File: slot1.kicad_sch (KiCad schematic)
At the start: 1 part

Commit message: board layout
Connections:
- net AD1: now also PL1.a3 (Pin_a3); no longer PL1.b3 (Pin_b3)
- net Chroma: now also PL1.a2 (Pin_a2); no longer PL1.b2 (Pin_b2)
- net GND: now also PL1.b3 (Pin_b3); no longer PL1.a3 (Pin_a3)
- net Luma: now also PL1.b2 (Pin_b2); no longer PL1.a2 (Pin_a2)
- net VCLK: now reaches PL1.a38 (Pin_a38)
- net ESND: now reaches PL1.b10 (Pin_b10)
- no-connect marks 1 -> 0

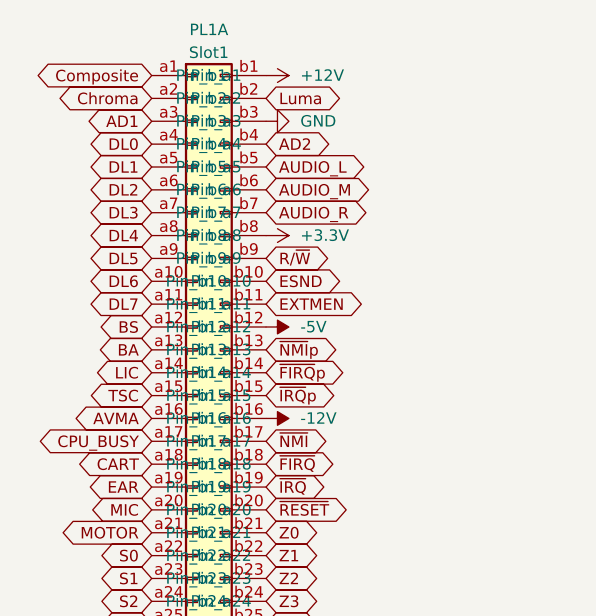
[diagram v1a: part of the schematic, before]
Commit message: revise bus tracing
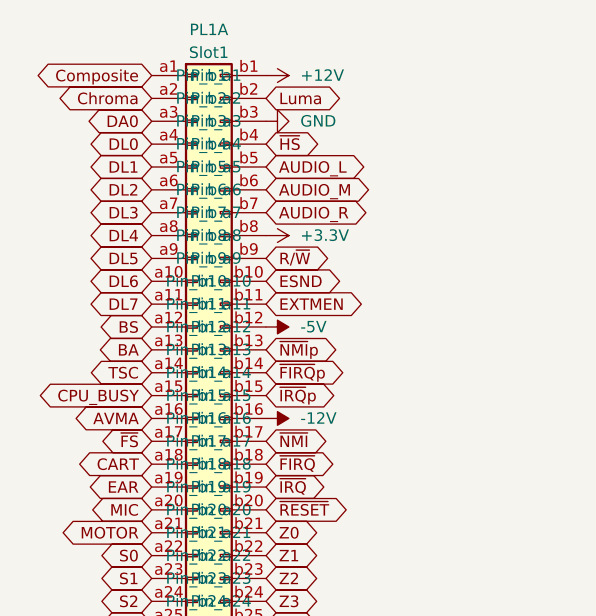
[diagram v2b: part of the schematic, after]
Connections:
- net LIC is gone; now on net TSC: PL1.a14 (Pin_a14)
- net CPU_BUSY: now also PL1.a15 (Pin_a15); no longer PL1.a17 (Pin_a17)
- net TSC: no longer PL1.a15 (Pin_a15)
- net AD1 renamed DA0
- net AD2 renamed ~{HS}
- new net ~{FS}: PL1.a17 (Pin_a17)
